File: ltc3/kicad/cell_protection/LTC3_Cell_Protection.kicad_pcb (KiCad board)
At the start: 4 copper layers, 92.2 x 68.9 mm, 245 parts, among them P1 XH header, P2 PIN_HEAD_1x2, P3 MicroFit header, P4 XH header, P7 MicroFit header, P8 MicroFit header, P9 XH header, Q1 SUM110P08-11, Q2 SUM110P08-11, Q3 NDS9407, Q4 SUM110P08-11, Q5 SUM110P08-11, Q6 MMBT3904, U1 BQ77PL900, U2 LTC2990

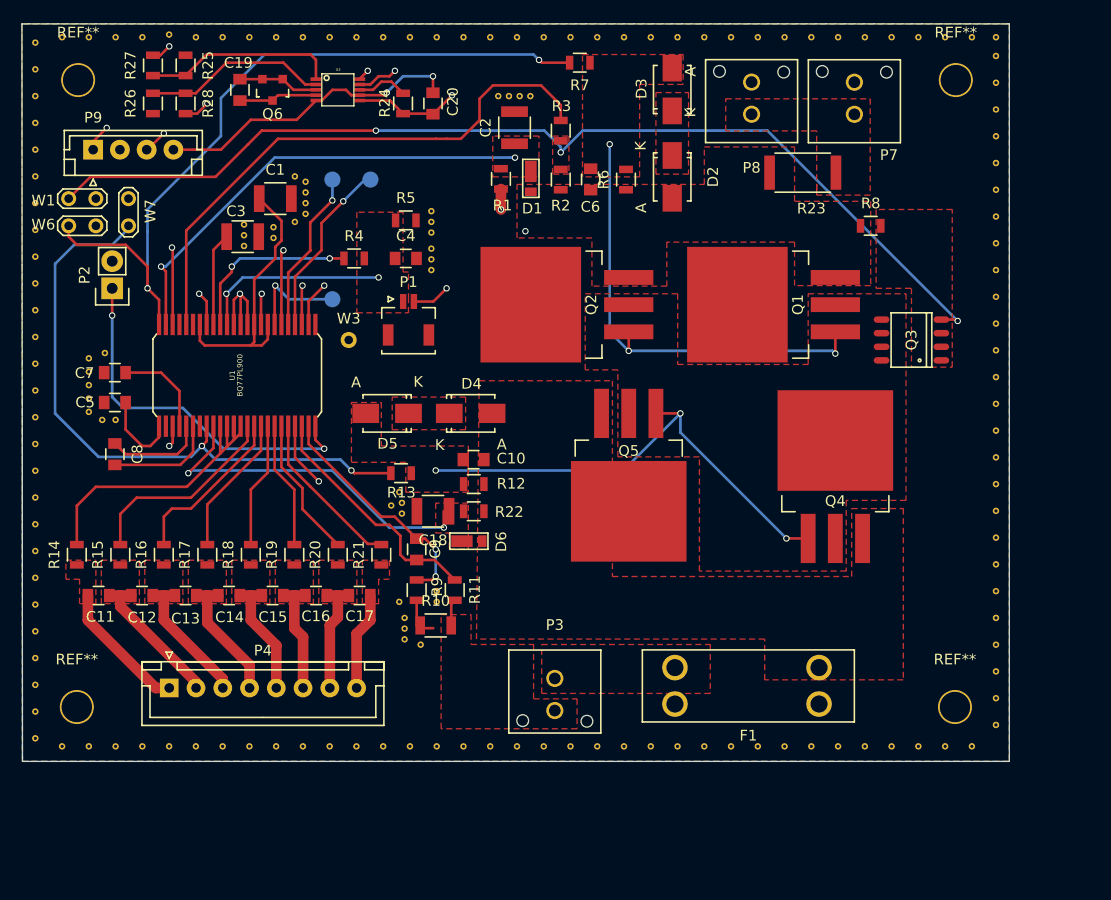
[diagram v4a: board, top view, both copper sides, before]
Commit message: LTC3 Layout Changes to Charge Controller/Cell Balancing
Finished up some changes on charge controller/cell balancing layout.
DRC gives zero errors, and everything is connected, huzzah!
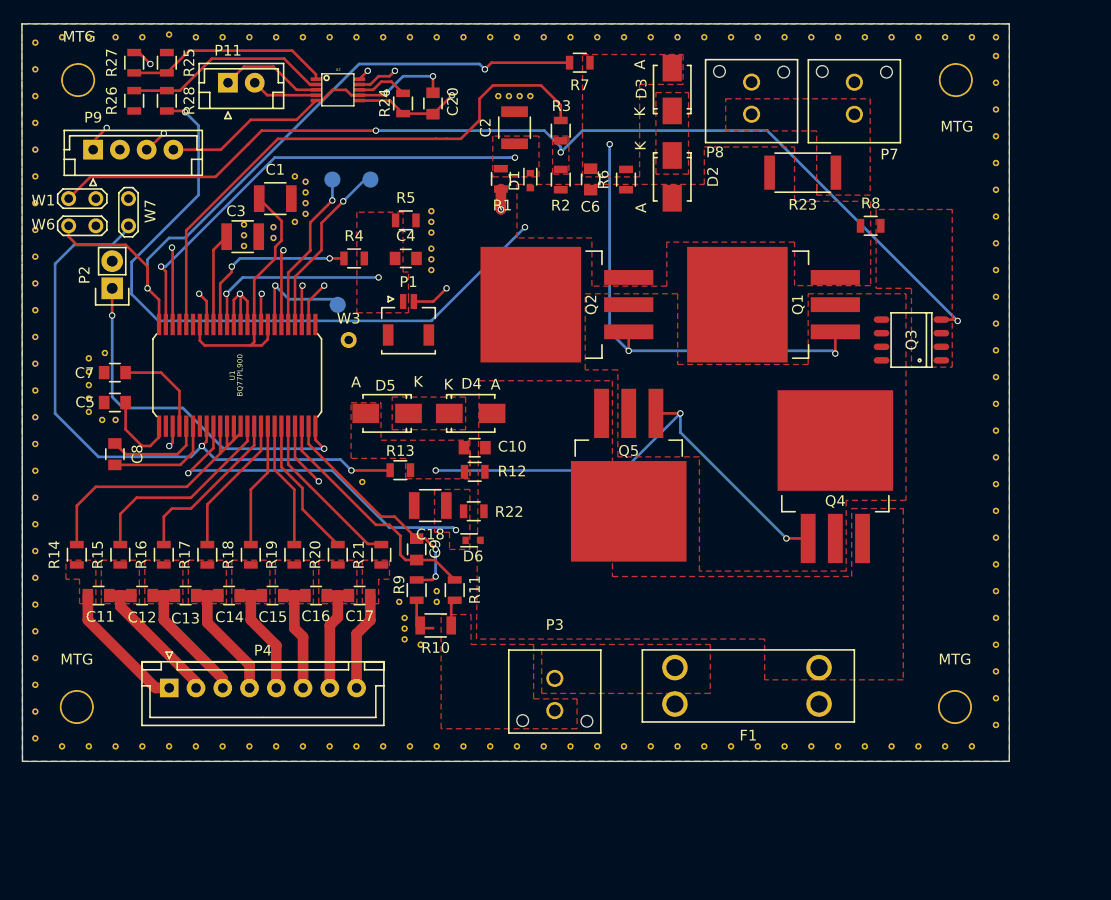
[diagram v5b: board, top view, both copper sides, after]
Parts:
- removed C19: 470p, Capacitors_SMD:C_0805
- removed Q6: MMBT3904, TO_SOT_Packages_SMD:SOT-23
- removed the REF** at (138.1, 109.7)
- removed the REF** at (139.1, 109.5)
- removed the REF** at (138.8, 108.5)
- added P11: XH header, Connectors_JST:JST_EH_B02B-EH-A_02x2.50mm_Straight, F.Cu at (122.8, 70.2)
- D1, D6: value 1SS355 -> CDSU4148; footprint Diodes_SMD:TUMD2 -> Diodes_SMD:SOD-523
- P2: value PIN_HEAD_1x2 -> pin header
- R4: value 6.89k -> 6.98k
- moved REF** 4.73 mm to (135.4, 107.5)
- moved R25 1.77 mm to (117.1, 68.3)
- moved R26 1.77 mm to (114.1, 71.9)
- moved R27 1.77 mm to (114.1, 68.3)
- moved R28 1.77 mm to (117.1, 71.9)
- moved R12 1.15 mm to (145.9, 106.5)
- moved C10 1.11 mm to (145.9, 104.3)
- moved W4 0.72 mm to (133.1, 91.0)
- moved C18 0.59 mm to (141.7, 109.7)
- moved R13 0.29 mm to (138.9, 106.4)
- moved D6 0.21 mm to (145.7, 113.0), turned to 180 degrees
- turned D1 to 90 degrees
- renumbered REF** to ?, REF** to MTG
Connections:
- U2 pad 3: (no net) -> Net-(P11-Pad1)
- U2 pad 4: (no net) -> Net-(P11-Pad2)
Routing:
- net Net-(C6-Pad1): track 47.5 -> 63.3 mm
- net Net-(P11-Pad1): track 0.00 -> 9.74 mm
- net Net-(C19-Pad1): track 7.51 -> 0.00 mm
- net Net-(C19-Pad2): track 7.31 -> 0.00 mm
- net Net-(P11-Pad2): track 0.00 -> 6.20 mm
- net Net-(R7-Pad2): track 70.6 -> 65.6 mm
- net Net-(R26-Pad2): track 17.4 -> 19.2 mm
- net Net-(R25-Pad2): track 18.1 -> 19.2 mm
- net /VBATT: track 75.9 -> 76.9 mm

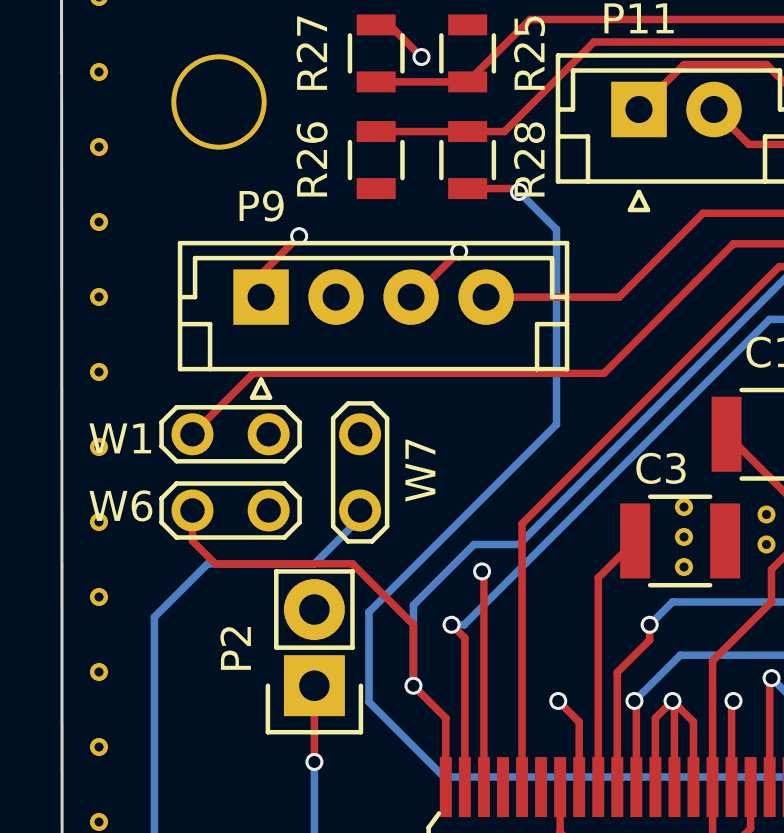
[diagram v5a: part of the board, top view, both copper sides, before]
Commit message: LTC3: Last Minute Layout Stuff
Some last minute changes on the charge controller/cell protection board.
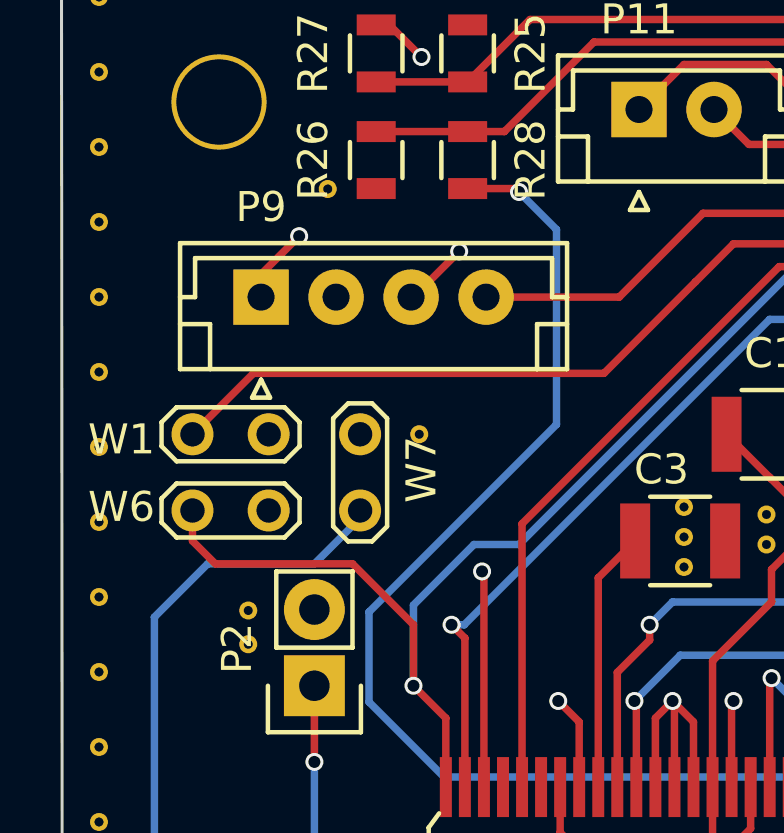
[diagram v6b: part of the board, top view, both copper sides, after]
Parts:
- added REF**: Via_.6mm, LTC3:Via_.6mm, F.Cu at (112.5, 72.8)
- added REF**: Via_.6mm, LTC3:Via_.6mm, F.Cu at (115.5, 81.0)
- added REF**: Via_.6mm, LTC3:Via_.6mm, F.Cu at (109.8, 88.0)
- added REF**: Via_.6mm, LTC3:Via_.6mm, F.Cu at (109.8, 86.9)
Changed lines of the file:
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@@
 (kicad_pcb (version 4) (host pcbnew "(2016-05-27 BZR 6836, Git 4441a4b)-product")
   (general
-    (links 319)
+    (links 323)
     (no_connects 0)
-    (area 103.533999 64.649999 195.884001 133.654001)
+    (area 98.441772 63.5487 201.104229 134.4863)
     (thickness 1.6)
     (drawings 4)
     (tracks 413)
     (zones 0)
-    (modules 241)
+    (modules 245)
     (nets 58)
   )
@@
     (35 F.Paste user)
     (36 B.SilkS user)
-    (37 F.SilkS user)
+    (37 F.SilkS user hide)
     (38 B.Mask user)
     (39 F.Mask user)
@@
     (add_net "Net-(U1-Pad31)")
   )
+  (module LTC3:Via_.6mm (layer F.Cu)
+    (at 112.459 72.85)
+    (fp_text reference REF** (at 0 1.27) (layer F.SilkS) hide
+      (effects (font (size 1 1) (thickness 0.15)))
+    )
+    (fp_text value Via_.6mm (at 0 -1.27) (layer F.Fab) hide
+      (effects (font (size 1 1) (thickness 0.15)))
+    )
+    (pad 1 thru_hole circle (at 0 0) (size 0.6 0.6) (drill 0.3) (layers *.Cu)
+      (net 1 GND) (zone_connect 2))
+  )
+  (module LTC3:Via_.6mm (layer F.Cu)
+    (at 115.509 81.025)
+    (fp_text reference REF** (at 0 1.27) (layer F.SilkS) hide
+      (effects (font (size 1 1) (thickness 0.15)))
+    )
+    (fp_text value Via_.6mm (at 0 -1.27) (layer F.Fab) hide
+      (effects (font (size 1 1) (thickness 0.15)))
+    )
+    (pad 1 thru_hole circle (at 0 0) (size 0.6 0.6) (drill 0.3) (layers *.Cu)
+      (net 1 GND) (zone_connect 2))
+  )
+  (module LTC3:Via_.6mm (layer F.Cu)
+    (at 109.809 88.025)
+    (fp_text reference REF** (at 0 1.27) (layer F.SilkS) hide
+      (effects (font (size 1 1) (thickness 0.15)))
+    )
+    (fp_text value Via_.6mm (at 0 -1.27) (layer F.Fab) hide
+      (effects (font (size 1 1) (thickness 0.15)))
+    )
+    (pad 1 thru_hole circle (at 0 0) (size 0.6 0.6) (drill 0.3) (layers *.Cu)
+      (net 1 GND) (zone_connect 2))
+  )
+  (module LTC3:Via_.6mm (layer F.Cu)
+    (at 109.809 86.9)
+    (fp_text reference REF** (at 0 1.27) (layer F.SilkS) hide
+      (effects (font (size 1 1) (thickness 0.15)))
+    )
+    (fp_text value Via_.6mm (at 0 -1.27) (layer F.Fab) hide
+      (effects (font (size 1 1) (thickness 0.15)))
+    )
+    (pad 1 thru_hole circle (at 0 0) (size 0.6 0.6) (drill 0.3) (layers *.Cu)
+      (net 1 GND) (zone_connect 2))
+  )
   (module Resistors_SMD:R_0805 (layer F.Cu)

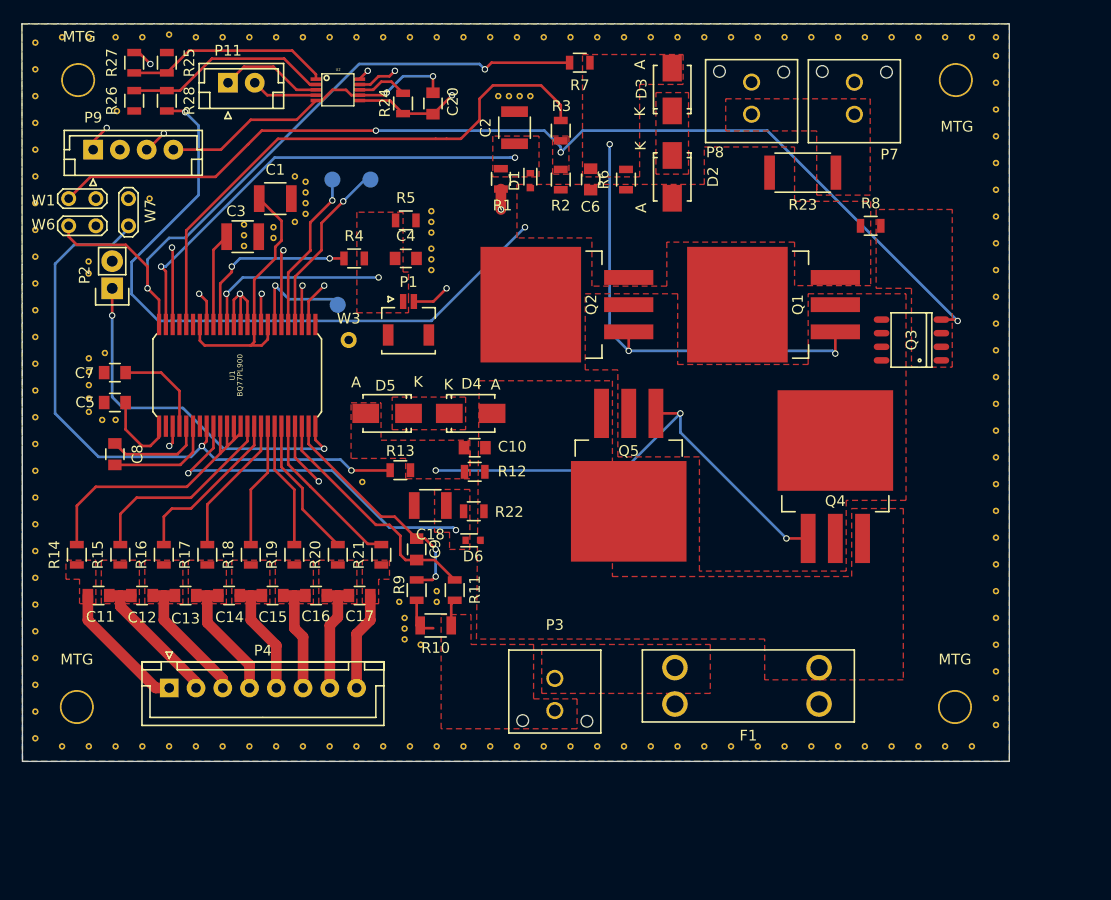
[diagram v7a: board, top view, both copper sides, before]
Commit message: LTC3: Layout Review Notes
-Connected pin 4 of connector
-Inserted two zero ohm resistors for SYNC/CHARGECFG2 pin
-Doubled up on input for Charge Controller board
-Added optoisolator to LT8490 board
-Made LTC2990 changes
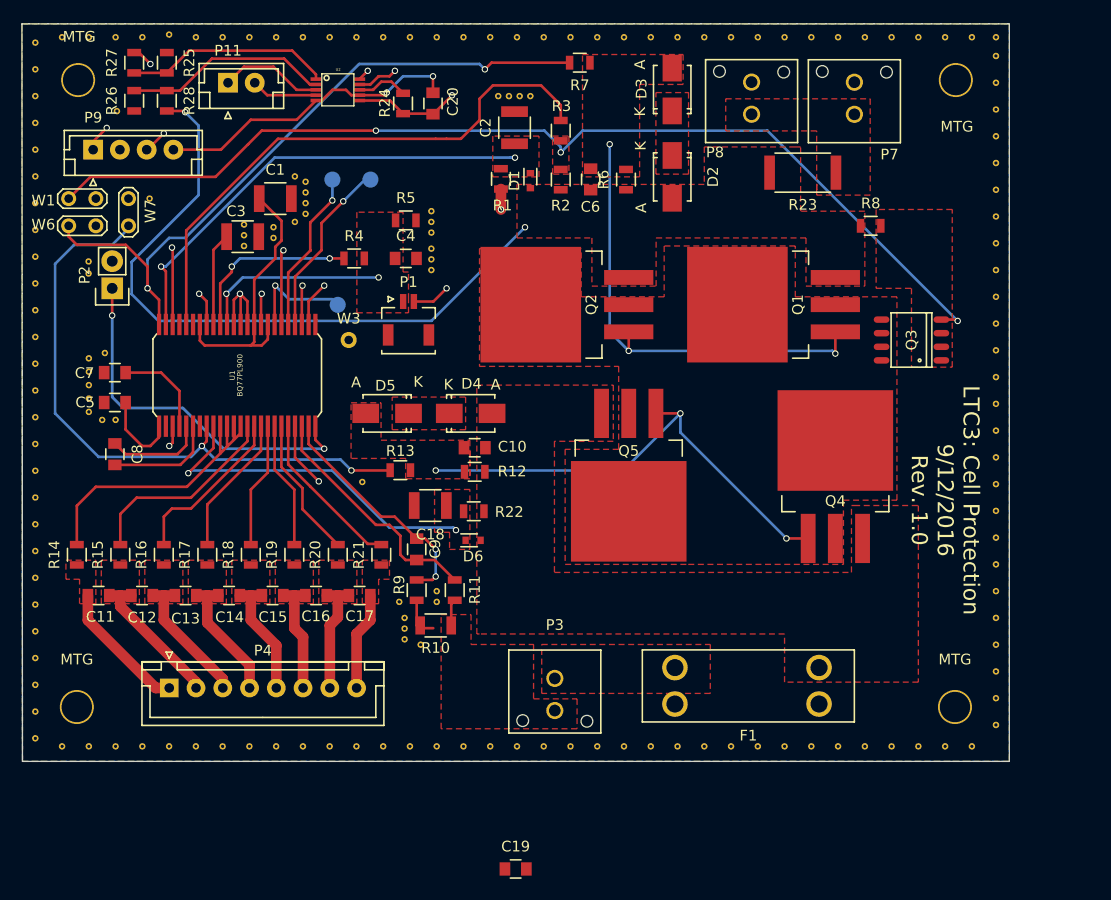
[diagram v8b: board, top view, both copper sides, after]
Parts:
- added C19: 470p, Capacitors_SMD:C_0805, F.Cu at (149.7, 143.7)
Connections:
- net +5V renamed Net-(C20-Pad1)
- Q1 pad 4: (no net) -> Net-(Q1-Pad2)
- Q2 pad 4: (no net) -> Net-(Q1-Pad2)
- Q4 pad 4: (no net) -> Net-(Q1-Pad2)
- Q5 pad 4: (no net) -> Net-(Q1-Pad2)
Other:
- board text added: "LTC3: Cell Protection 9/12/2016 Rev. 1.0"
